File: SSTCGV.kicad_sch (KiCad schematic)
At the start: 46 parts, among them IC1 ATTINY13-20PU, J1-1 INPUT 1, J1-2 INPUT 2, J2 COILS, J3 POWER, J4 OPT, Q1 IRLZ44N, Q2 IRLZ44N, Q3 IRLZ44N, SW1 SW_Push_DPDT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

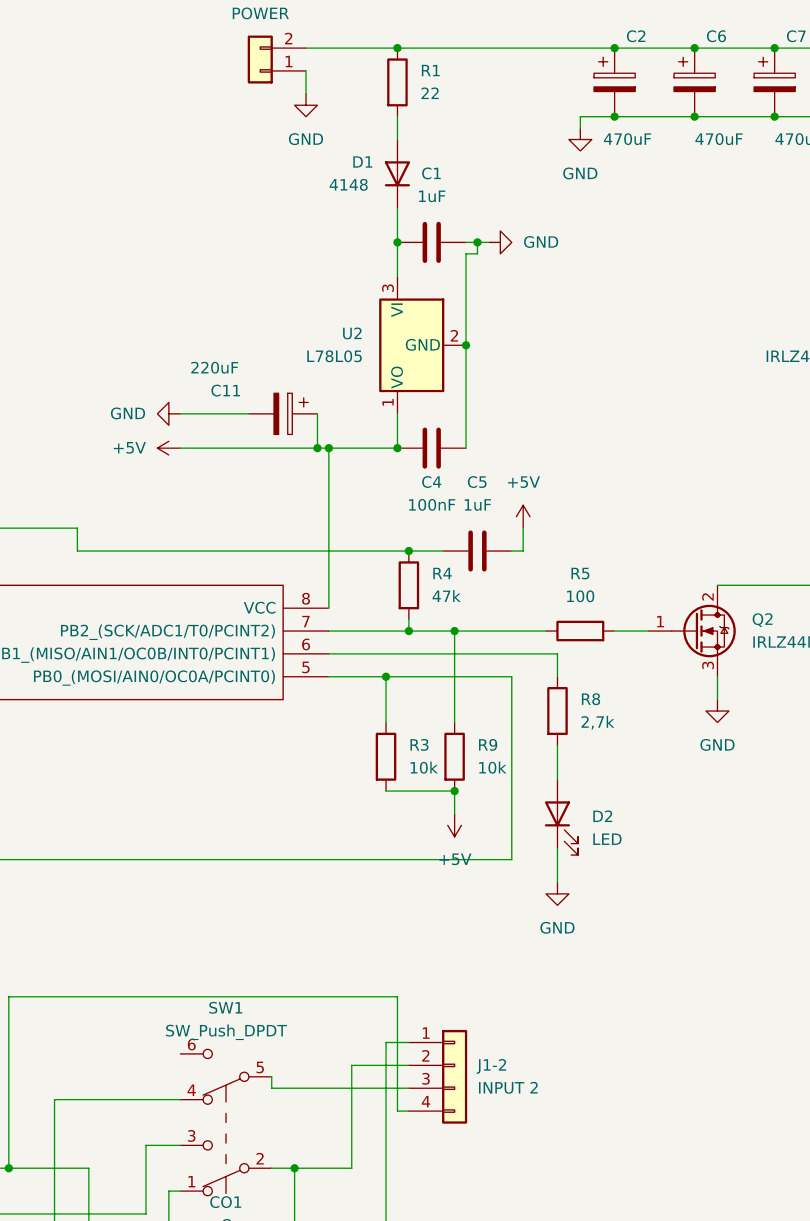
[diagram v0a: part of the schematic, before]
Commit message: corrections of schematics
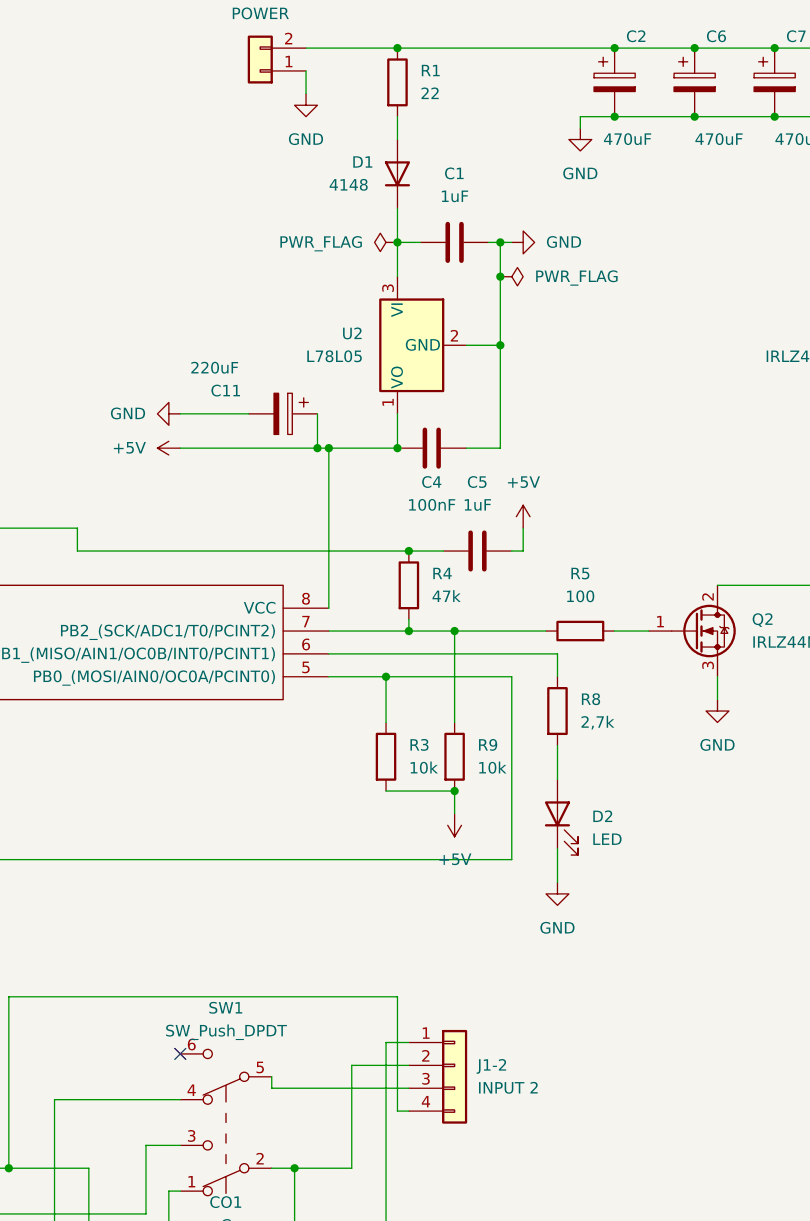
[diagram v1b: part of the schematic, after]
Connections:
- no-connect marks 0 -> 1
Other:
- moved on the sheet: C1

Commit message: woking on pcb
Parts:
- removed J1-1: INPUT 1, Connector_PinSocket_2.54mm:PinSocket_1x04_P2.54mm_Vertical, symbol Connector_Generic:Conn_01x04
- removed J1-2: INPUT 2, Connector_PinSocket_2.54mm:PinSocket_1x04_P2.54mm_Vertical, symbol Connector_Generic:Conn_01x04
- D2: footprint LED_THT:LED_D5.0mm-3_Horizontal_O3.81mm_Z3.0mm -> LED_THT:LED_D5.0mm-3
- R1: footprint Resistor_THT:R_Axial_DIN0411_L9.9mm_D3.6mm_P15.24mm_Horizontal -> Resistor_THT:R_Axial_DIN0309_L9.0mm_D3.2mm_P5.08mm_Vertical
- R2, R3, R4, R5, R6, R8, R9, RO1, RO2: footprint Resistor_THT:R_Axial_DIN0411_L9.9mm_D3.6mm_P15.24mm_Horizontal -> Resistor_THT:R_Axial_DIN0411_L9.9mm_D3.6mm_P7.62mm_Vertical
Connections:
- net +5V: now also RV2.3, U1.4
- net GND: now also CO1.2, RO2.2, RV2.1, SW1.2 (B)
- net at C3.1, IC1.3 ((PCINT4/ADC2)_PB4), R2.1: now also SW1.5 (B)
- net at IC1.5 (PB0_(MOSI/AIN0/OC0A/PCINT0)), R3.1: now also CO1.1, SW1.1 (A)

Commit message: franta scheme approve
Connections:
- net at RO2.1, U1.3: now also SW1.6 (C); no longer SW1.3 (C)
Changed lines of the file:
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@@
   (junction (at 157.48 88.9) (diameter 0) (color 0 0 0 0)
   )
-  (no_connect (at 132.08 144.78))
+  (no_connect (at 132.08 154.94))
   (wire (pts (xy 73.66 162.56) (xy 73.66 161.29))
     (stroke (width 0) (type default) (color 0 0 0 0))
@@
     (stroke (width 0) (type default) (color 0 0 0 0))
   )
-  (wire (pts (xy 105.41 162.56) (xy 128.27 162.56))
+  (wire (pts (xy 105.41 162.56) (xy 115.57 162.56))
     (stroke (width 0) (type default) (color 0 0 0 0))
   )
@@
     (stroke (width 0) (type default) (color 0 0 0 0))
   )
+  (wire (pts (xy 115.57 144.78) (xy 115.57 162.56))
+    (stroke (width 0) (type default) (color 0 0 0 0))
+  )
   (wire (pts (xy 85.09 120.65) (xy 85.09 115.57))
     (stroke (width 0) (type default) (color 0 0 0 0))
@@
     (stroke (width 0) (type default) (color 0 0 0 0))
   )
+  (wire (pts (xy 118.11 149.86) (xy 132.08 149.86))
+    (stroke (width 0) (type default) (color 0 0 0 0))
+  )
   (wire (pts (xy 130.81 160.02) (xy 132.08 160.02))
     (stroke (width 0) (type default) (color 0 0 0 0))
@@
     (stroke (width 0) (type default) (color 0 0 0 0))
   )
-  (wire (pts (xy 118.11 149.86) (xy 132.08 149.86))
-    (stroke (width 0) (type default) (color 0 0 0 0))
-  )
   (wire (pts (xy 144.78 157.48) (xy 151.13 157.48))
     (stroke (width 0) (type default) (color 0 0 0 0))
@@
     (stroke (width 0) (type default) (color 0 0 0 0))
   )
-  (wire (pts (xy 128.27 154.94) (xy 132.08 154.94))
+  (wire (pts (xy 115.57 144.78) (xy 132.08 144.78))
     (stroke (width 0) (type default) (color 0 0 0 0))
   )
@@
     (stroke (width 0) (type default) (color 0 0 0 0))
   )
-  (wire (pts (xy 128.27 162.56) (xy 128.27 154.94))
-    (stroke (width 0) (type default) (color 0 0 0 0))
-  )
